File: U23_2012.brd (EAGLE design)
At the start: 160 x 100 mm, 53 parts, among them X2 J1006F01P

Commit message: adds misc page
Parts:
- added C12, C13, C4: 100n, rcl:C025-024X044
- added LED1, LED2, LED3, LED4, LED5: (no value), led:LED3MM
- added R24, R25, R26, R27, R28: 1k, rcl:0207/10
- added R29, R30, R31, R32, R33, R34: 10k, rcl:0207/10
- added S1, S2, S3, S4, S5, S6: (no value), switch-omron:B3F-10XX
- added T1: BC337, transistor:TO92
- added TP1, TP2: TPTP20SQ, testpad:TP20SQ
- C1, C10, C11, C2, C5, C6, C7, C9: value 0.1µF -> 100n
- C3: value 0.01µF -> 10n; device rcl:SMC_C -> rcl:C0603
- C8: value 10µF -> 10u
- U$5: value (none) -> 50Mhz
- moved C3 277.8 mm to (-157.5, -166.4)
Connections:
- removed net N$30: U$2.CD
- new net N$14: LED1.A, R24.1
- new net N$15: LED2.A, R25.1
- new net N$16: LED3.A, R26.1
- new net N$17: LED4.A, R27.1
- new net N$18: LED5.A, R28.1
- new net N$20: T1.3, TP1.TP
- net 3V: now also C3.2, C4.2, TP2.TP; no longer C3.+
- net 5V: now also C12.1, C13.1, R28.2, S1.1, S1.2, S2.1, S2.2, S3.1, S3.2, S4.1, S4.2, S5.1, S5.2, S6.1, S6.2
- net GND: now also C3.1, LED1.K, LED2.K, LED3.K, LED4.K, LED5.K, R29.1, R30.1, R31.1, R32.1, R33.1, R34.1, T1.1; no longer C3.-
- net PB0: now also R34.2, S6.3, S6.4
- net PB1: now also R33.2, S5.3, S5.4
- net PB2: now also U$2.CD
- net PB4: now also R29.2, S2.3, S2.4
- net PB5: now also R31.2, S3.3, S3.4
- net PB7: now also R30.2, S1.3, S1.4
- net PB8: now also R32.2, S4.3, S4.4
- net PD1: no longer U$4.3
- net PD12: now also R24.2
- net PD13: now also R25.2
- net PD14: now also R26.2
- net PD15: now also R27.2
- net PD3: no longer U$4.2
- net PD6: now also U$4.3
- net PD7: now also U$4.2

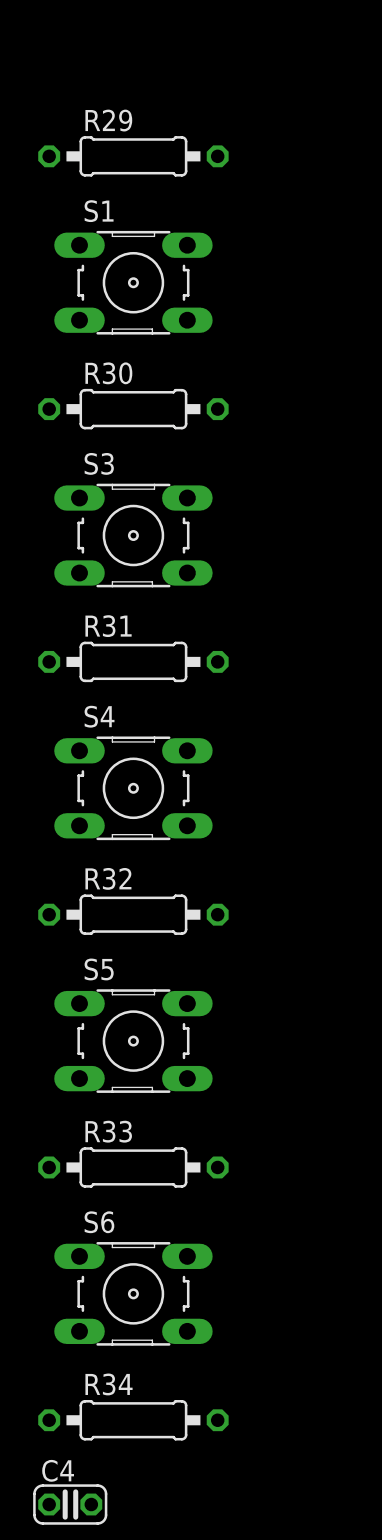
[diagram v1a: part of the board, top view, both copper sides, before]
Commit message: removes pulldowns of buttons, due to internal pulldowns of MCU. Reexports netlist etc.
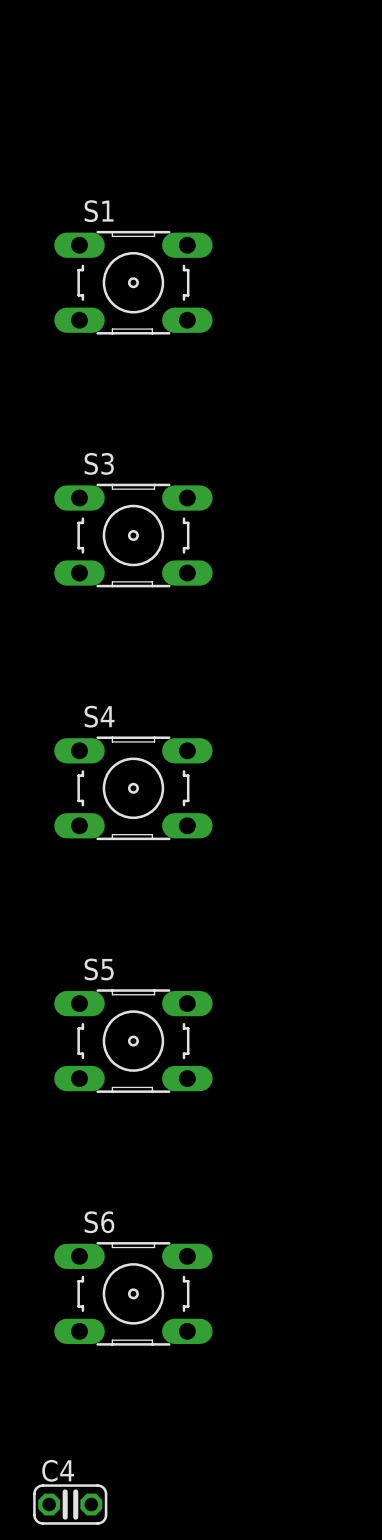
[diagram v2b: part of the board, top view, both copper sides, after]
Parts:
- removed R29, R30, R31, R32, R33, R34: 10k, rcl:0207/10
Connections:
- net GND: no longer R29.1, R30.1, R31.1, R32.1, R33.1, R34.1
- net PB0: no longer R34.2
- net PB1: no longer R33.2
- net PB4: no longer R29.2
- net PB5: no longer R31.2
- net PB7: no longer R30.2
- net PB8: no longer R32.2
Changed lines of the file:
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@@
 <attribute name="OC_FARNELL" value="176432" x="-109.22" y="-57.15" size="1.778" layer="27" display="off"/>
 </element>
-<element name="R29" library="rcl" package="0207/10" value="10k" x="-153.67" y="-67.31"/>
 <element name="S1" library="switch-omron" package="B3F-10XX" value="" x="-153.67" y="-74.93">
 <attribute name="OC_NEWARK" value="36M3542" x="-165.1" y="-62.23" size="1.778" layer="27" display="off"/>
@@
 <attribute name="OC_FARNELL" value="176432" x="-165.1" y="-62.23" size="1.778" layer="27" display="off"/>
 </element>
-<element name="R30" library="rcl" package="0207/10" value="10k" x="-153.67" y="-82.55"/>
 <element name="S3" library="switch-omron" package="B3F-10XX" value="" x="-153.67" y="-90.17">
 <attribute name="OC_NEWARK" value="36M3542" x="-165.1" y="-77.47" size="1.778" layer="27" display="off"/>
@@
 <attribute name="OC_FARNELL" value="176432" x="-165.1" y="-77.47" size="1.778" layer="27" display="off"/>
 </element>
-<element name="R31" library="rcl" package="0207/10" value="10k" x="-153.67" y="-97.79"/>
 <element name="S4" library="switch-omron" package="B3F-10XX" value="" x="-153.67" y="-105.41">
 <attribute name="OC_NEWARK" value="36M3542" x="-165.1" y="-92.71" size="1.778" layer="27" display="off"/>
@@
 <attribute name="OC_FARNELL" value="176432" x="-165.1" y="-92.71" size="1.778" layer="27" display="off"/>
 </element>
-<element name="R32" library="rcl" package="0207/10" value="10k" x="-153.67" y="-113.03"/>
 <element name="S5" library="switch-omron" package="B3F-10XX" value="" x="-153.67" y="-120.65">
 <attribute name="OC_NEWARK" value="36M3542" x="-165.1" y="-107.95" size="1.778" layer="27" display="off"/>
@@
 <attribute name="OC_FARNELL" value="176432" x="-165.1" y="-107.95" size="1.778" layer="27" display="off"/>
 </element>
-<element name="R33" library="rcl" package="0207/10" value="10k" x="-153.67" y="-128.27"/>
 <element name="S6" library="switch-omron" package="B3F-10XX" value="" x="-153.67" y="-135.89">
 <attribute name="OC_NEWARK" value="36M3542" x="-165.1" y="-123.19" size="1.778" layer="27" display="off"/>
@@
 <attribute name="OC_FARNELL" value="176432" x="-165.1" y="-123.19" size="1.778" layer="27" display="off"/>
 </element>
-<element name="R34" library="rcl" package="0207/10" value="10k" x="-153.67" y="-143.51"/>
 <element name="C4" library="rcl" package="C025-024X044" value="100n" x="-157.48" y="-148.59"/>
 <element name="C12" library="rcl" package="C025-024X044" value="100n" x="-157.48" y="-154.94"/>
@@
 <contactref element="LED3" pad="K"/>
 <contactref element="LED4" pad="K"/>
-<contactref element="R29" pad="1"/>
-<contactref element="R30" pad="1"/>
-<contactref element="R31" pad="1"/>
-<contactref element="R32" pad="1"/>
-<contactref element="R33" pad="1"/>
-<contactref element="R34" pad="1"/>
 <contactref element="C3" pad="1"/>
 <contactref element="T1" pad="1"/>
-<wire x1="-158.75" y1="-67.31" x2="-158.75" y2="-82.55" width="0" layer="19" extent="1-1"/>
-<wire x1="-158.75" y1="-97.79" x2="-158.75" y2="-82.55" width="0" layer="19" extent="1-1"/>
-<wire x1="-158.75" y1="-113.03" x2="-158.75" y2="-97.79" width="0" layer="19" extent="1-1"/>
-<wire x1="-158.75" y1="-128.27" x2="-158.75" y2="-113.03" width="0" layer="19" extent="1-1"/>
-<wire x1="-158.75" y1="-143.51" x2="-158.75" y2="-128.27" width="0" layer="19" extent="1-1"/>
-<wire x1="-158.33" y1="-166.37" x2="-158.75" y2="-143.51" width="0" layer="19" extent="1-1"/>
-<wire x1="-154.94" y1="-172.72" x2="-158.33" y2="-166.37" width="0" layer="19" extent="1-1"/>
-<wire x1="-88.9" y1="-35.56" x2="-158.75" y2="-67.31" width="0" layer="19" extent="1-1"/>
 <wire x1="-88.9" y1="-30.48" x2="-88.9" y2="-35.56" width="0" layer="19" extent="1-1"/>
 <wire x1="-88.9" y1="-25.4" x2="-88.9" y2="-30.48" width="0" layer="19" extent="1-1"/>
@@
 <wire x1="-15.84" y1="5.08" x2="-40.04" y2="5.08" width="0" layer="19" extent="1-1"/>
 <wire x1="-13.54" y1="8.38" x2="-15.84" y2="5.08" width="0" layer="19" extent="1-1"/>
+<wire x1="-158.33" y1="-166.37" x2="-88.9" y2="-35.56" width="0" layer="19" extent="1-1"/>
+<wire x1="-154.94" y1="-172.72" x2="-158.33" y2="-166.37" width="0" layer="19" extent="1-1"/>
 </signal>
 <signal name="PE15">
@@
 <contactref element="S1" pad="3"/>
 <contactref element="S1" pad="4"/>
-<contactref element="R30" pad="2"/>
 <wire x1="-150.4188" y1="-77.1906" x2="-156.9212" y2="-77.1906" width="0" layer="19" extent="1-1"/>
-<wire x1="-148.59" y1="-82.55" x2="-150.4188" y2="-77.1906" width="0" layer="19" extent="1-1"/>
 <wire x1="-52.07" y1="74.93" x2="-150.4188" y2="-77.1906" width="0" layer="19" extent="1-1"/>
 </signal>
@@
 <contactref element="S3" pad="3"/>
 <contactref element="S3" pad="4"/>
-<contactref element="R31" pad="2"/>
 <wire x1="-150.4188" y1="-92.4306" x2="-156.9212" y2="-92.4306" width="0" layer="19" extent="1-1"/>
-<wire x1="-148.59" y1="-97.79" x2="-150.4188" y2="-92.4306" width="0" layer="19" extent="1-1"/>
 <wire x1="-49.53" y1="74.93" x2="-150.4188" y2="-92.4306" width="0" layer="19" extent="1-1"/>
 </signal>
@@
 <contactref element="S2" pad="3"/>
 <contactref element="S2" pad="4"/>
-<contactref element="R29" pad="2"/>
-<wire x1="-112.4712" y1="-59.4106" x2="-148.59" y2="-67.31" width="0" layer="19" extent="1-1"/>
 <wire x1="-105.9688" y1="-59.4106" x2="-112.4712" y2="-59.4106" width="0" layer="19" extent="1-1"/>
 <wire x1="-49.53" y1="72.39" x2="-105.9688" y2="-59.4106" width="0" layer="19" extent="1-1"/>
@@
 <contactref element="S4" pad="3"/>
 <contactref element="S4" pad="4"/>
-<contactref element="R32" pad="2"/>
 <wire x1="-150.4188" y1="-107.6706" x2="-57.15" y2="72.39" width="0" layer="19" extent="1-1"/>
-<wire x1="-148.59" y1="-113.03" x2="-150.4188" y2="-107.6706" width="0" layer="19" extent="1-1"/>
 <wire x1="-156.9212" y1="-107.6706" x2="-150.4188" y2="-107.6706" width="0" layer="19" extent="1-1"/>
 </signal>
@@
 <contactref element="S6" pad="3"/>
 <contactref element="S6" pad="4"/>
-<contactref element="R34" pad="2"/>
 <wire x1="-150.4188" y1="-138.1506" x2="-156.9212" y2="-138.1506" width="0" layer="19" extent="1-1"/>
-<wire x1="-148.59" y1="-143.51" x2="-150.4188" y2="-138.1506" width="0" layer="19" extent="1-1"/>
 <wire x1="-54.61" y1="62.23" x2="-150.4188" y2="-138.1506" width="0" layer="19" extent="1-1"/>
 </signal>
@@
 <contactref element="S5" pad="3"/>
 <contactref element="S5" pad="4"/>
-<contactref element="R33" pad="2"/>
 <wire x1="-150.4188" y1="-122.9106" x2="-156.9212" y2="-122.9106" width="0" layer="19" extent="1-1"/>
-<wire x1="-148.59" y1="-128.27" x2="-150.4188" y2="-122.9106" width="0" layer="19" extent="1-1"/>
 <wire x1="-54.61" y1="59.69" x2="-150.4188" y2="-122.9106" width="0" layer="19" extent="1-1"/>
 </signal>

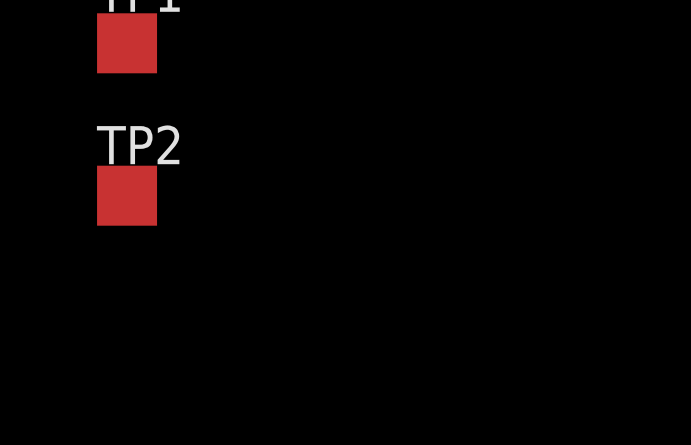
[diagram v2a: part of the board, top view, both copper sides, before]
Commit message: adds missing base resistor to T1
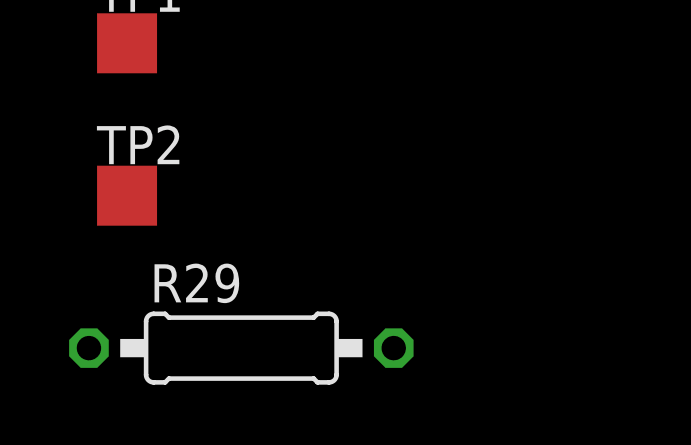
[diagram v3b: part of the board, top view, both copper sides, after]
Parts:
- added R29: 270, rcl:0207/10
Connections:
- new net N$19: R29.2, T1.2
- net PD8: now also R29.1
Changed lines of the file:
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@@
 <attribute name="TP_SIGNAL_NAME" value="" x="-157.48" y="-182.88" size="1.778" layer="27" display="off"/>
 </element>
+<element name="R29" library="rcl" package="0207/10" value="270" x="-153.67" y="-187.96"/>
 </elements>
 <signals>
@@
 <signal name="PD8">
 <contactref element="SV1" pad="40"/>
+<contactref element="R29" pad="1"/>
+<wire x1="-31.75" y1="62.23" x2="-158.75" y2="-187.96" width="0" layer="19" extent="1-1"/>
 </signal>
 <signal name="PD10">
@@
 <wire x1="-157.48" y1="-172.72" x2="-157.48" y2="-177.8" width="0" layer="19" extent="1-1"/>
 </signal>
+<signal name="N$19">
+<contactref element="T1" pad="2"/>
+<contactref element="R29" pad="2"/>
+<wire x1="-156.21" y1="-170.815" x2="-148.59" y2="-187.96" width="0" layer="19" extent="1-1"/>
+</signal>
 </signals>

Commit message: board rev 0.1
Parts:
- removed U$10, U$11, U$12, U$13, U$14, U$6, U$7, U$8, U$9: DO_WHAT_I_WANT, library:NONE
- RN1, RN2: device resistor-dil:0603-ARV -> resistor-dil:CAR06ES
- moved R29 387.4 mm to (140.7, 64.0), turned to 180 degrees
- moved TP2 378.7 mm to (138.0, 54.0), turned to 90 degrees
- moved TP1 373.2 mm to (135.0, 54.0), turned to 90 degrees
- moved T1 372.9 mm to (135.8, 59.3)
- moved C3 346.7 mm to (77.0, 89.0)
- moved S6 343.9 mm to (143.0, 38.0)
- moved S5 322.0 mm to (134.0, 24.0)
- moved C13 288.1 mm to (79.0, 4.52), turned to 90 degrees
- moved C4 276.6 mm to (36.6, 48.5), turned to 90 degrees
- moved C12 246.8 mm to (30.9, 4.52), turned to 90 degrees
- moved R28 238.9 mm to (140.0, 14.0), turned to 90 degrees
- moved R27 234.4 mm to (137.0, 14.0), turned to 90 degrees
- moved LED5 228.6 mm to (135.0, 4.00), turned to 180 degrees
- moved LED4 222.9 mm to (130.0, 4.00), turned to 180 degrees
- moved S4 209.2 mm to (5.00, 31.0)
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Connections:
- removed net CRS_DV: R16.1, U$1.40, U$8.A
- removed net MDC: U$1.31, U$9.A
- removed net MDIO: U$1.30, U$7.A
- removed net OSCIN: U$1.34, U$5.OUT, U$6.A
- removed net RXD0: U$1.43, U$10.A
- removed net RXD1: U$1.44, U$11.A
- removed net TXD0: U$1.3, U$13.A
- removed net TXD1: U$1.4, U$14.A
- removed net TX_EN: U$1.2, U$12.A
- net 3V: now also RN1.A2, RN1.B2, RN1.C2; no longer RN1.6, RN1.7, RN1.8
- net GND: now also C12.2, C13.2, C4.1, R9.2
- net N$1: now also RN2.D2; no longer RN2.5
- net N$10: now also RN2.A1, RN2.B1, RN2.C1, RN2.D1; no longer RN2.1, RN2.2, RN2.3, RN2.4
- net N$2: now also RN2.C2; no longer RN2.6
- net N$3: now also RN2.B2; no longer RN2.7
- net N$4: now also RN2.A2; no longer RN2.8
- net N$5: now also RN1.A1; no longer RN1.1
- net N$6: now also RN1.C1; no longer RN1.3
- net N$7: now also RN1.B1; no longer RN1.2
- net PA1: now also U$1.34, U$5.OUT; no longer U$6.B
- net PA2: now also U$1.30; no longer U$7.B
- net PA7: now also R16.1, U$1.40; no longer U$8.B
- net PB11: now also U$1.2; no longer U$12.B
- net PB12: now also U$1.3; no longer U$13.B
- net PB13: now also U$1.4; no longer U$14.B
- net PC1: now also U$1.31; no longer U$9.B
- net PC4: now also U$1.43; no longer U$10.B
- net PC5: now also U$1.44; no longer U$11.B
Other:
- board size 160 x 100 mm -> 150 x 100 mm

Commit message: fixes wrong routed signal
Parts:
- moved RN1 3.61 mm to (47.0, 76.0)
- moved RN2 0.50 mm to (46.5, 86.5), turned to 180 degrees
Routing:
- net GND: track 0.00 -> 639.4 mm
- net 5V: track 0.00 -> 302.9 mm, vias 0 -> 1
- net 3V: track 0.00 -> 256.5 mm, vias 0 -> 4
- net PD12: track 0.00 -> 168.3 mm
- net PD14: track 0.00 -> 150.8 mm
- net PB12: track 0.00 -> 126.2 mm, vias 0 -> 1
- net PB11: track 0.00 -> 122.8 mm, vias 0 -> 2
- net PB7: track 0.00 -> 122.2 mm, vias 0 -> 1
- net PE7: track 0.00 -> 121.5 mm, vias 0 -> 1
- net PC11: track 0.00 -> 119.6 mm
- net PB13: track 0.00 -> 118.5 mm, vias 0 -> 2
- net PC9: track 0.00 -> 118.0 mm, vias 0 -> 2
- net PB5: track 0.00 -> 114.3 mm, vias 0 -> 1
- net PC8: track 0.00 -> 109.2 mm, vias 0 -> 1
- net PC5: track 0.00 -> 108.2 mm, vias 0 -> 5
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- added copper zone on layer 1, net GND
- added copper zone on layer 16, net GND
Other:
- board text added: "REV 0.1"

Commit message: adds connector to http://www.wvshare.com/product/DP83848-Ethernet-Board.htm Ethernet boards switches position of LED1 and LED5 adds silkscreen annotations etc removes pdf and drill files
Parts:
- added SV3: (no value), con-harting-ml:ML20L
- moved LED1 149.3 mm to (136.0, 4.00)
- moved LED5 148.5 mm to (6.00, 77.5)
- moved R28 140.2 mm to (15.0, 77.5), turned to 0 degrees
- moved R24 140.1 mm to (140.0, 14.0), turned to 90 degrees
- moved S1 2.00 mm to (14.0, 38.0)
- moved S2 2.00 mm to (21.0, 31.0)
- moved S3 2.00 mm to (14.0, 24.0)
- moved S4 2.00 mm to (7.00, 31.0)
- moved U$1 0.05 mm to (58.0, 87.0)
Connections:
- net 3V: now also SV3.1, SV3.2
- net GND: now also SV3.3, SV3.4
- net PA2: now also SV3.5
- net PA7: now also SV3.8
- net PB11: now also SV3.11
- net PB12: now also SV3.12
- net PB13: now also SV3.13
- net PC1: now also SV3.6
- net PC4: now also SV3.9
- net PC5: now also SV3.10
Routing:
- net PD12: track 168.3 -> 38.1 mm, vias 0 -> 1
- net PC1: track 85.7 -> 188.8 mm
- net PC5: track 108.2 -> 177.9 mm, vias 5 -> 9
- net PA7: track 104.0 -> 161.2 mm
- net 5V: track 302.9 -> 351.0 mm
- net PC4: track 91.7 -> 131.4 mm, vias 3 -> 5
- net PB13: track 118.5 -> 145.2 mm, vias 2 -> 3
- net PB11: track 122.8 -> 145.0 mm, vias 2 -> 3
- net GND: track 639.4 -> 653.6 mm, vias 0 -> 5
- net PA2: track 98.7 -> 112.4 mm
- net PB12: track 126.2 -> 136.7 mm
- net 3V: track 256.5 -> 261.5 mm
- net N$18: track 6.60 -> 2.65 mm
- net N$14: track 3.18 -> 6.19 mm
- net PB8: track 98.4 -> 96.4 mm
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- added copper zone on layer 16, net N$21
- removed copper zone on layer 16, net GND
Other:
- board text added: "A"
- board text added: "B"
- board text added: "CHAOS COMPUTER CLUB COLOGNE"
- board text added: "DOWN"
- board text added: "ETHERNET"
- board text added: "LED A"
- board text added: "LED B"
- board text added: "LEFT"
- board text added: "POWER"
- board text added: "R2R DAC"
- board text added: "REV 1.0"
- board text added: "RIGHT"
- board text added: "RUMBLE"
- board text added: "SD CARD"
- board text added: "SNES 1"
- board text added: "SNES 2"
- board text added: "SSTM32"
- board text added: "UP"
- board text added: "VGA"
- board text removed: "REV 0.1"

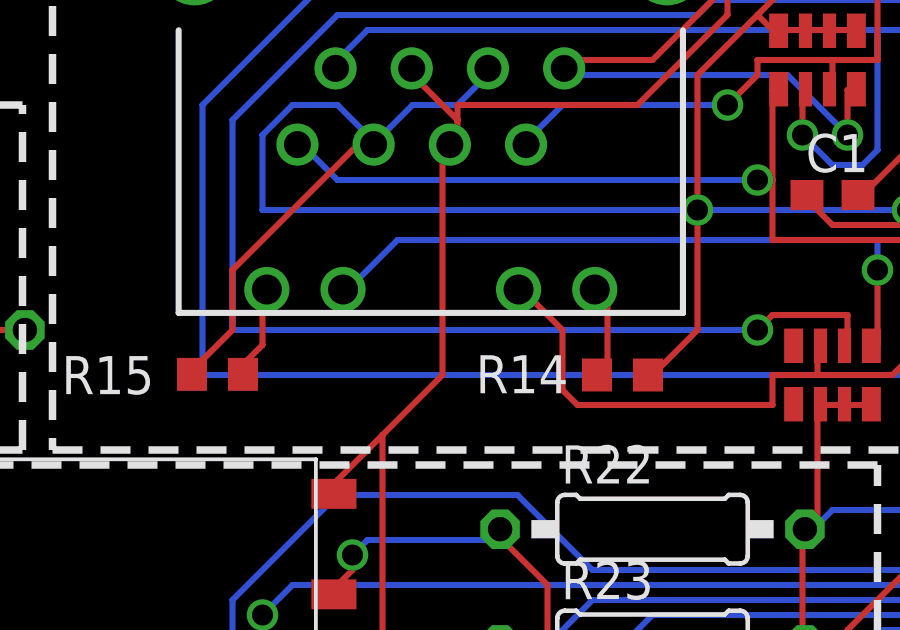
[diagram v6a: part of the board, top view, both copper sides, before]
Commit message: removes stupid mistake on ethernet jack
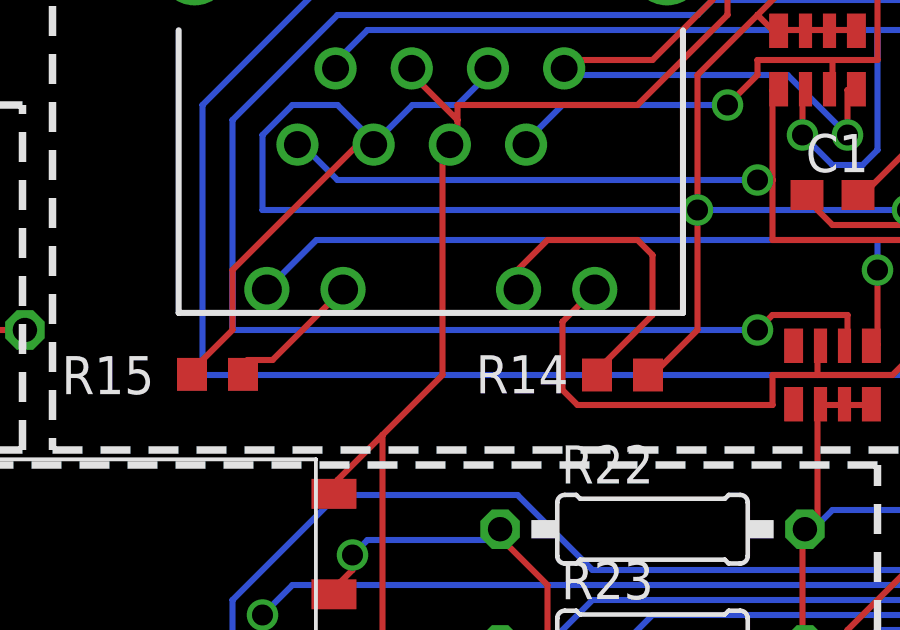
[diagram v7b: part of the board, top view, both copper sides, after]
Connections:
- net N$12: now also X2.10; no longer X2.9
- net N$13: now also X2.11; no longer X2.12
- net N$5: now also X2.9; no longer X2.10
- net N$6: now also X2.12; no longer X2.11
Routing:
- net N$13: track 3.40 -> 10.9 mm
- net N$5: track 32.2 -> 34.8 mm
- net N$12: track 3.09 -> 4.66 mm
